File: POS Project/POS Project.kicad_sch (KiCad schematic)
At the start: 60 parts, among them J1 JST_2mm_LiPo, J2 Conn_01x05_Socket, P1 USB_C_Plug_USB2.0, SW1 SW_Push, SW2 SW_Push, U1 SIM7600x, U2 MCP73831-2-OT, U3 SMN-303, U4 SMF05C, U5 GSM_ANT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

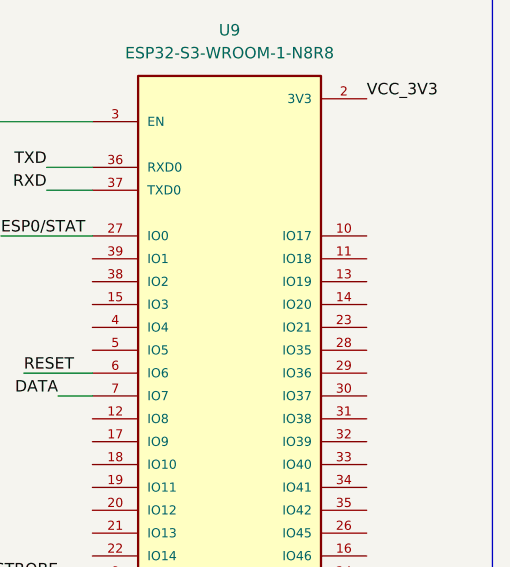
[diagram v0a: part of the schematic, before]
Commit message: added PCB routs
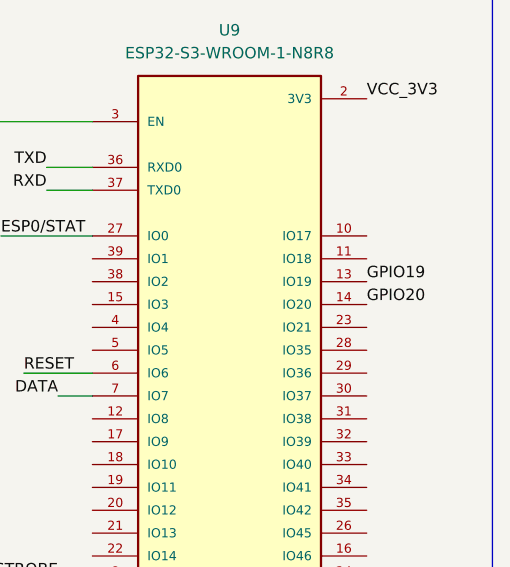
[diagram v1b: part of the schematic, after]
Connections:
- net GPIO19: now also U9.13 (IO19)
- net GPIO20: now also U9.14 (IO20)
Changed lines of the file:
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@@
+		)
+	)
+	(label "GPIO20"
+		(at 372.11 54.61 0)
+		(effects
+			(font
+				(size 1.27 1.27)
+			)
+			(justify left bottom)
 		)
 	)
@@
 		(effects
 			(font
+				(size 1.27 1.27)
+			)
+			(justify left bottom)
+		)
+	)
+	(label "GPIO19"
+		(at 372.11 52.07 0)
+		(effects
+			(font
